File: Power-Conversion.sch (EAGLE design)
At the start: 25 parts, among them Q1 SUM90P10-19L, U7 LM2678

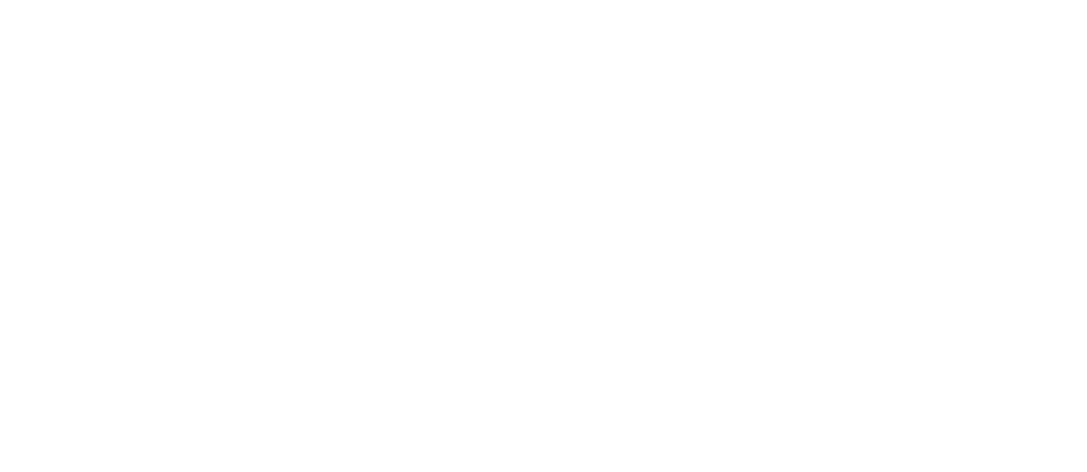
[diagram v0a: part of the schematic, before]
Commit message: added current sense
added current sense and support things
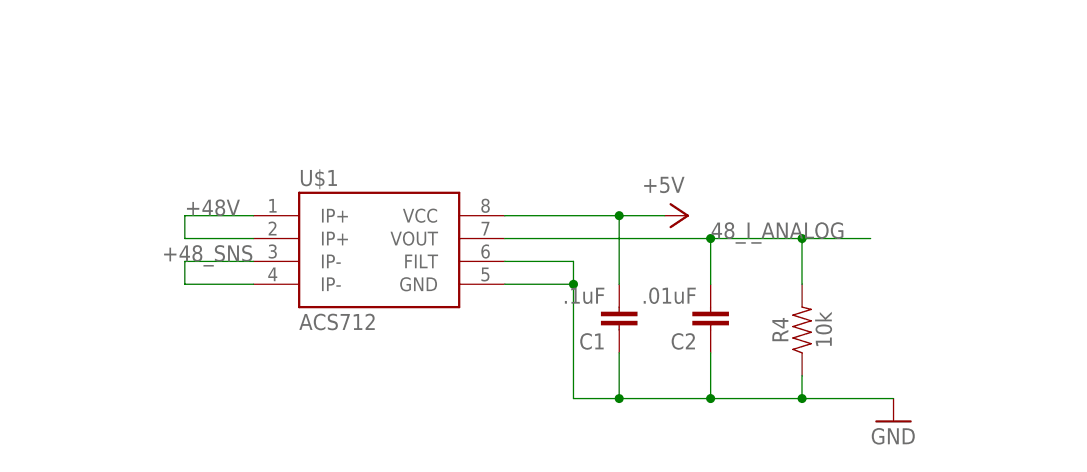
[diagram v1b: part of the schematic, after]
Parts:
- added C1: .1uF, SparkFun-Capacitors:4.7UF0603
- added C2: .01uF, SparkFun-Capacitors:4.7UF0603
- added R4: 10k, SparkFun-Resistors:10KOHM-0603-1/10W-1%
- added U$1: ACS712, SparkFun-Sensors:ACS712
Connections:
- new net +48_SNS: U$1.IP-@3, U$1.IP-@4
- new net 48_I_ANALOG: C2.2, R4.2, U$1.VOUT
- net +48V: now also U$1.IP+@1, U$1.IP+@2
- net +5V: now also C1.2, U$1.VCC
- net GND: now also C1.1, C2.1, R4.1, U$1.FILT, U$1.GND
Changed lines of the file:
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@@
 <attribute name="PARTNO" value="SUM90P10-19L-E3CT-ND"/>
 </part>
+<part name="U$1" library="SparkFun-Sensors" deviceset="ACS712" device="" value="ACS712"/>
+<part name="C1" library="SparkFun-Capacitors" deviceset="4.7UF" device="0603" value=".1uF"/>
+<part name="C2" library="SparkFun-Capacitors" deviceset="4.7UF" device="0603" value=".01uF"/>
+<part name="R4" library="SparkFun-Resistors" deviceset="10KOHM" device="-0603-1/10W-1%" value="10k"/>
+<part name="GND2" library="supply1" deviceset="GND" device=""/>
+<part name="P+5" library="supply1" deviceset="+5V" device=""/>
 </parts>
 <sheets>
@@
 <attribute name="BOM" value="INCLUDE" x="116.84" y="193.04" size="0.0254" layer="96" font="vector" rot="MR0" display="off"/>
 </instance>
+<instance part="U$1" gate="G$1" x="147.32" y="109.22"/>
+<instance part="C1" gate="G$1" x="172.72" y="104.14" rot="R180"/>
+<instance part="C2" gate="G$1" x="182.88" y="104.14" rot="R180"/>
+<instance part="R4" gate="G$1" x="193.04" y="101.6" rot="R90"/>
+<instance part="GND2" gate="1" x="203.2" y="91.44"/>
+<instance part="P+5" gate="1" x="180.34" y="114.3" rot="R270"/>
 </instances>
 <busses>
@@
 <pinref part="GND1" gate="1" pin="GND"/>
 </segment>
+<segment>
+<pinref part="U$1" gate="G$1" pin="GND"/>
+<wire x1="160.02" y1="106.68" x2="167.64" y2="106.68" width="0.1524" layer="91"/>
+<wire x1="167.64" y1="106.68" x2="167.64" y2="93.98" width="0.1524" layer="91"/>
+<pinref part="GND2" gate="1" pin="GND"/>
+<wire x1="167.64" y1="93.98" x2="172.72" y2="93.98" width="0.1524" layer="91"/>
+<wire x1="172.72" y1="93.98" x2="182.88" y2="93.98" width="0.1524" layer="91"/>
+<pinref part="U$1" gate="G$1" pin="FILT"/>
+<wire x1="182.88" y1="93.98" x2="193.04" y2="93.98" width="0.1524" layer="91"/>
+<wire x1="193.04" y1="93.98" x2="203.2" y2="93.98" width="0.1524" layer="91"/>
+<wire x1="160.02" y1="109.22" x2="167.64" y2="109.22" width="0.1524" layer="91"/>
+<wire x1="167.64" y1="109.22" x2="167.64" y2="106.68" width="0.1524" layer="91"/>
+<pinref part="C1" gate="G$1" pin="1"/>
+<wire x1="172.72" y1="93.98" x2="172.72" y2="99.06" width="0.1524" layer="91"/>
+<pinref part="C2" gate="G$1" pin="1"/>
+<wire x1="182.88" y1="99.06" x2="182.88" y2="93.98" width="0.1524" layer="91"/>
+<pinref part="R4" gate="G$1" pin="1"/>
+<wire x1="193.04" y1="96.52" x2="193.04" y2="93.98" width="0.1524" layer="91"/>
+</segment>
 </net>
 <net name="ONOFF" class="0">
@@
 <wire x1="238.76" y1="185.42" x2="238.76" y2="177.8" width="0.1524" layer="91"/>
 </segment>
+<segment>
+<pinref part="U$1" gate="G$1" pin="VCC"/>
+<pinref part="P+5" gate="1" pin="+5V"/>
+<wire x1="160.02" y1="114.3" x2="172.72" y2="114.3" width="0.1524" layer="91"/>
+<pinref part="C1" gate="G$1" pin="2"/>
+<wire x1="172.72" y1="114.3" x2="177.8" y2="114.3" width="0.1524" layer="91"/>
+<wire x1="172.72" y1="106.68" x2="172.72" y2="114.3" width="0.1524" layer="91"/>
+</segment>
 </net>
 <net name="N$25" class="0">
@@
 <wire x1="121.92" y1="195.58" x2="129.54" y2="195.58" width="0.1524" layer="91"/>
 <label x="134.62" y="195.58" size="1.778" layer="95"/>
+</segment>
+<segment>
+<pinref part="U$1" gate="G$1" pin="IP+@1"/>
+<wire x1="132.08" y1="114.3" x2="124.46" y2="114.3" width="0.1524" layer="91"/>
+<pinref part="U$1" gate="G$1" pin="IP+@2"/>
+<wire x1="132.08" y1="111.76" x2="124.46" y2="111.76" width="0.1524" layer="91"/>
+<wire x1="124.46" y1="114.3" x2="124.46" y2="111.76" width="0.1524" layer="91"/>
+<label x="124.46" y="114.3" size="1.778" layer="95"/>
 </segment>
 </net>
@@
 </segment>
 </net>
+<net name="+48_SNS" class="0">
+<segment>
+<pinref part="U$1" gate="G$1" pin="IP-@3"/>
+<wire x1="132.08" y1="109.22" x2="124.46" y2="109.22" width="0.1524" layer="91"/>
+<pinref part="U$1" gate="G$1" pin="IP-@4"/>
+<wire x1="132.08" y1="106.68" x2="124.46" y2="106.68" width="0.1524" layer="91"/>
+<wire x1="124.46" y1="109.22" x2="124.46" y2="106.68" width="0.1524" layer="91"/>
+<label x="121.92" y="109.22" size="1.778" layer="95"/>
+</segment>
+</net>
+<net name="48_I_ANALOG" class="0">
+<segment>
+<pinref part="U$1" gate="G$1" pin="VOUT"/>
+<wire x1="160.02" y1="111.76" x2="182.88" y2="111.76" width="0.1524" layer="91"/>
+<label x="182.88" y="111.76" size="1.778" layer="95"/>
+<pinref part="C2" gate="G$1" pin="2"/>
+<wire x1="182.88" y1="111.76" x2="193.04" y2="111.76" width="0.1524" layer="91"/>
+<wire x1="193.04" y1="111.76" x2="200.66" y2="111.76" width="0.1524" layer="91"/>
+<wire x1="182.88" y1="106.68" x2="182.88" y2="111.76" width="0.1524" layer="91"/>
+<pinref part="R4" gate="G$1" pin="2"/>
+<wire x1="193.04" y1="106.68" x2="193.04" y2="111.76" width="0.1524" layer="91"/>
+</segment>
+</net>
+<net name="GND1" class="0">
+<segment>
+<junction x="172.72" y="114.3"/>
+</segment>
+</net>
+<net name="GND2" class="0">
+<segment>
+<junction x="172.72" y="93.98"/>
+</segment>
+</net>
+<net name="GND3" class="0">
+<segment>
+<junction x="182.88" y="93.98"/>
+</segment>
+</net>
+<net name="GND4" class="0">
+<segment>
+<junction x="182.88" y="111.76"/>
+</segment>
+</net>
+<net name="GND5" class="0">
+<segment>
+<junction x="193.04" y="111.76"/>
+</segment>
+</net>
+<net name="GND6" class="0">
+<segment>
+<junction x="193.04" y="93.98"/>
+</segment>
+</net>
+<net name="GND7" class="0">
+<segment>
+<junction x="167.64" y="106.68"/>
+</segment>
+</net>

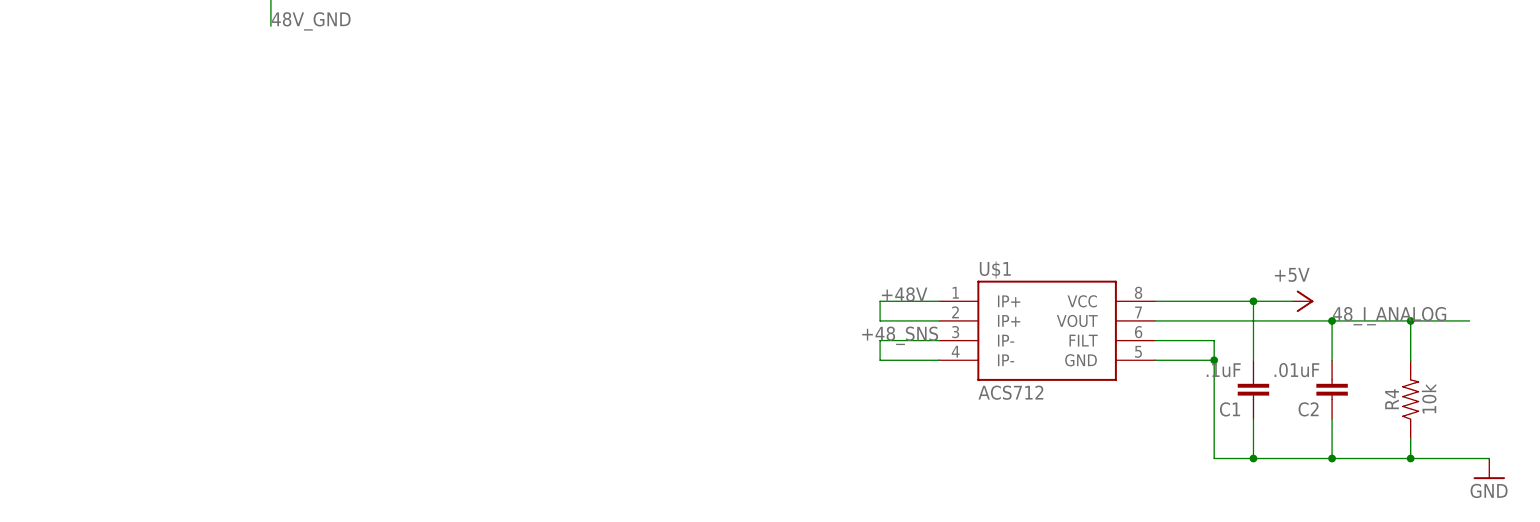
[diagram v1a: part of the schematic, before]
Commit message: Added voltage connectors
added the voltage connectors
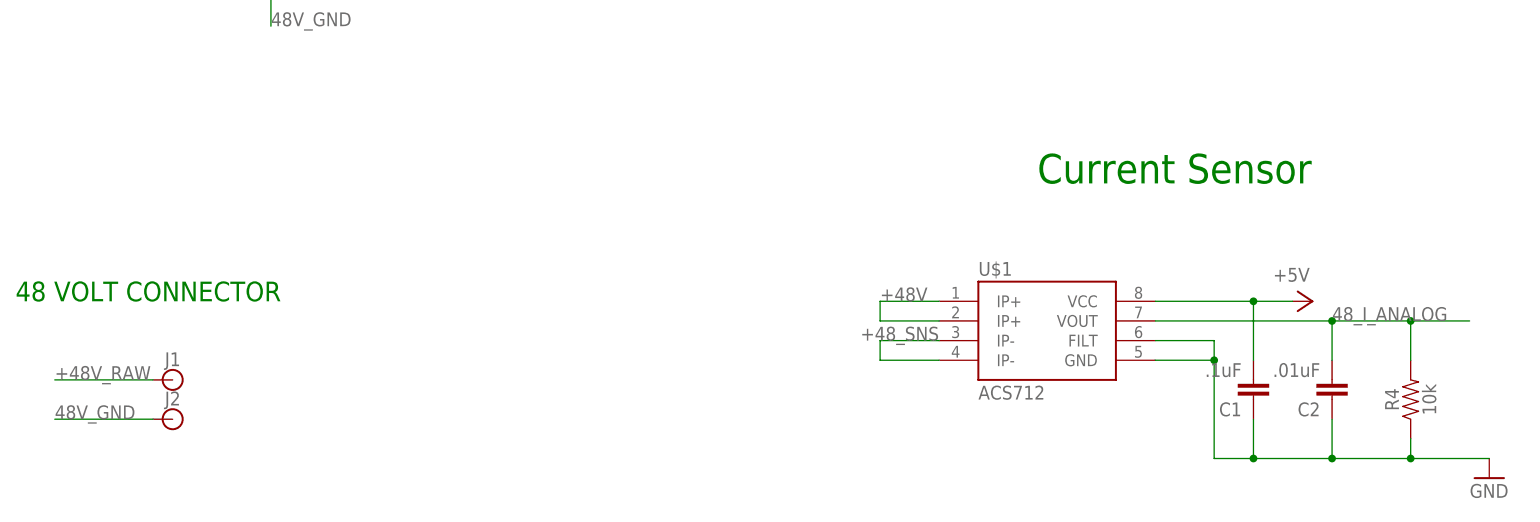
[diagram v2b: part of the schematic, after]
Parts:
- added J1, J2: (no value), SparkFun-Connectors:BANANA_CONN
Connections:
- net +48V_RAW: now also J1.1
- net 48V_GND: now also J2.1
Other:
- note added: "48 VOLT CONNECTOR"
- note added: "Current Sensor"
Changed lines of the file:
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@@
 <part name="GND2" library="supply1" deviceset="GND" device=""/>
 <part name="P+5" library="supply1" deviceset="+5V" device=""/>
+<part name="J1" library="SparkFun-Connectors" deviceset="BANANA_CONN" device=""/>
+<part name="J2" library="SparkFun-Connectors" deviceset="BANANA_CONN" device=""/>
 </parts>
 <sheets>
@@
 <text x="20.32" y="205.74" size="3.81" layer="91">Turn on switch</text>
 <text x="96.52" y="210.82" size="3.81" layer="91">reverse voltage protection</text>
+<text x="12.7" y="114.3" size="2.54" layer="91">48 VOLT CONNECTOR</text>
+<text x="144.78" y="129.54" size="3.81" layer="91">Current Sensor</text>
 </plain>
 <instances>
@@
 <instance part="GND2" gate="1" x="203.2" y="91.44"/>
 <instance part="P+5" gate="1" x="180.34" y="114.3" rot="R270"/>
+<instance part="J1" gate="G$1" x="33.02" y="104.14"/>
+<instance part="J2" gate="G$1" x="33.02" y="99.06"/>
 </instances>
 <busses>
@@
 <label x="119.38" y="157.48" size="1.778" layer="95"/>
 </segment>
+<segment>
+<pinref part="J2" gate="G$1" pin="1"/>
+<wire x1="30.48" y1="99.06" x2="17.78" y2="99.06" width="0.1524" layer="91"/>
+<label x="17.78" y="99.06" size="1.778" layer="95"/>
+</segment>
 </net>
 <net name="+12V" class="0">
@@
 <label x="99.06" y="203.2" size="1.778" layer="95"/>
 </segment>
-</net>
+<segment>
+<pinref part="J1" gate="G$1" pin="1"/>
+<wire x1="30.48" y1="104.14" x2="17.78" y2="104.14" width="0.1524" layer="91"/>
+<label x="17.78" y="104.14" size="1.778" layer="95"/>
+</segment>
+</net>

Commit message: added Connectors
added connectors to schematic
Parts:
- added U$2: SAMTEC-10, SAMTEC-10:SAMTEC-10
- added U$3, U$8: POWER-BRICK-CONNECTOR, MotherboardParts:POWER-BRICK-CONNECTOR
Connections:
- new net 12V: U$3.P$2, U$8.P$1
- net GND: now also U$3.P$1, U$8.P$2
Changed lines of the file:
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@@
 <part name="J1" library="SparkFun-Connectors" deviceset="BANANA_CONN" device=""/>
 <part name="J2" library="SparkFun-Connectors" deviceset="BANANA_CONN" device=""/>
+<part name="U$3" library="MotherboardParts" deviceset="POWER-BRICK-CONNECTOR" device=""/>
+<part name="U$8" library="MotherboardParts" deviceset="POWER-BRICK-CONNECTOR" device=""/>
+<part name="GND3" library="supply1" deviceset="GND" device=""/>
+<part name="GND4" library="supply1" deviceset="GND" device=""/>
+<part name="SUPPLY1" library="SparkFun-PowerSymbols" deviceset="12V" device=""/>
+<part name="SUPPLY2" library="SparkFun-PowerSymbols" deviceset="12V" device=""/>
+<part name="U$2" library="SAMTEC-10" deviceset="SAMTEC-10" device=""/>
 </parts>
 <sheets>
@@
 <instance part="R4" gate="G$1" x="193.04" y="101.6" rot="R90"/>
 <instance part="GND2" gate="1" x="203.2" y="91.44"/>
-<instance part="P+5" gate="1" x="180.34" y="114.3" rot="R270"/>
+<instance part="P+5" gate="1" x="172.72" y="124.46"/>
 <instance part="J1" gate="G$1" x="33.02" y="104.14"/>
 <instance part="J2" gate="G$1" x="33.02" y="99.06"/>
+<instance part="U$3" gate="G$1" x="83.82" y="421.64"/>
+<instance part="U$8" gate="G$1" x="83.82" y="452.12"/>
+<instance part="GND3" gate="1" x="101.6" y="421.64"/>
+<instance part="GND4" gate="1" x="101.6" y="436.88"/>
+<instance part="SUPPLY1" gate="G$1" x="109.22" y="421.64"/>
+<instance part="SUPPLY2" gate="G$1" x="109.22" y="464.82"/>
+<instance part="U$2" gate="G$1" x="81.28" y="492.76"/>
 </instances>
 <busses>
@@
 <wire x1="193.04" y1="96.52" x2="193.04" y2="93.98" width="0.1524" layer="91"/>
 </segment>
+<segment>
+<pinref part="U$8" gate="G$1" pin="P$2"/>
+<wire x1="96.52" y1="444.5" x2="101.6" y2="444.5" width="0.1524" layer="91"/>
+<pinref part="GND4" gate="1" pin="GND"/>
+<wire x1="101.6" y1="444.5" x2="101.6" y2="439.42" width="0.1524" layer="91"/>
+</segment>
+<segment>
+<pinref part="U$3" gate="G$1" pin="P$1"/>
+<wire x1="96.52" y1="429.26" x2="101.6" y2="429.26" width="0.1524" layer="91"/>
+<pinref part="GND3" gate="1" pin="GND"/>
+<wire x1="101.6" y1="429.26" x2="101.6" y2="424.18" width="0.1524" layer="91"/>
+</segment>
 </net>
 <net name="ONOFF" class="0">
@@
 <wire x1="160.02" y1="114.3" x2="172.72" y2="114.3" width="0.1524" layer="91"/>
 <pinref part="C1" gate="G$1" pin="2"/>
-<wire x1="172.72" y1="114.3" x2="177.8" y2="114.3" width="0.1524" layer="91"/>
+<wire x1="172.72" y1="114.3" x2="172.72" y2="121.92" width="0.1524" layer="91"/>
 <wire x1="172.72" y1="106.68" x2="172.72" y2="114.3" width="0.1524" layer="91"/>
 </segment>
@@
 </segment>
 </net>
+<net name="12V" class="0">
+<segment>
+<pinref part="U$3" gate="G$1" pin="P$2"/>
+<wire x1="96.52" y1="414.02" x2="109.22" y2="414.02" width="0.1524" layer="91"/>
+<pinref part="SUPPLY1" gate="G$1" pin="12V"/>
+<wire x1="109.22" y1="414.02" x2="109.22" y2="421.64" width="0.1524" layer="91"/>
+</segment>
+<segment>
+<pinref part="U$8" gate="G$1" pin="P$1"/>
+<wire x1="96.52" y1="459.74" x2="109.22" y2="459.74" width="0.1524" layer="91"/>
+<pinref part="SUPPLY2" gate="G$1" pin="12V"/>
+<wire x1="109.22" y1="459.74" x2="109.22" y2="464.82" width="0.1524" layer="91"/>
+</segment>
+</net>

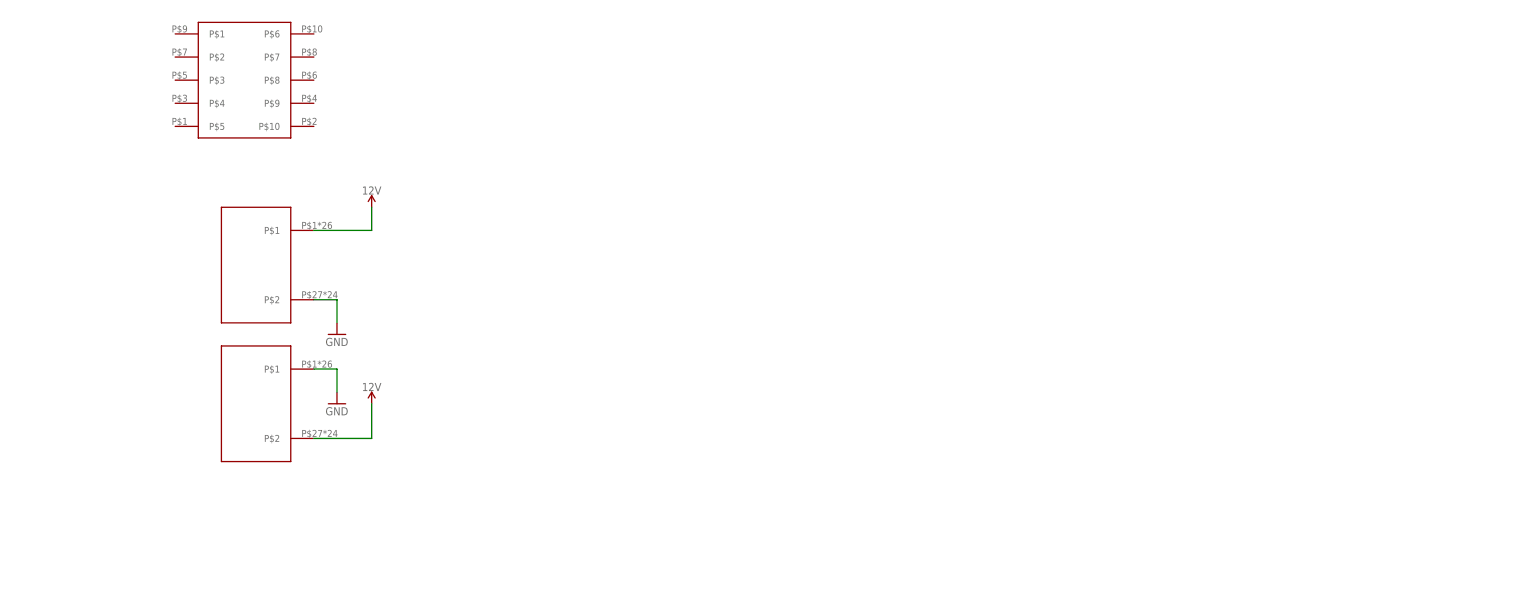
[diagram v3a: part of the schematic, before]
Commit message: Added micro
added the microcontroller.
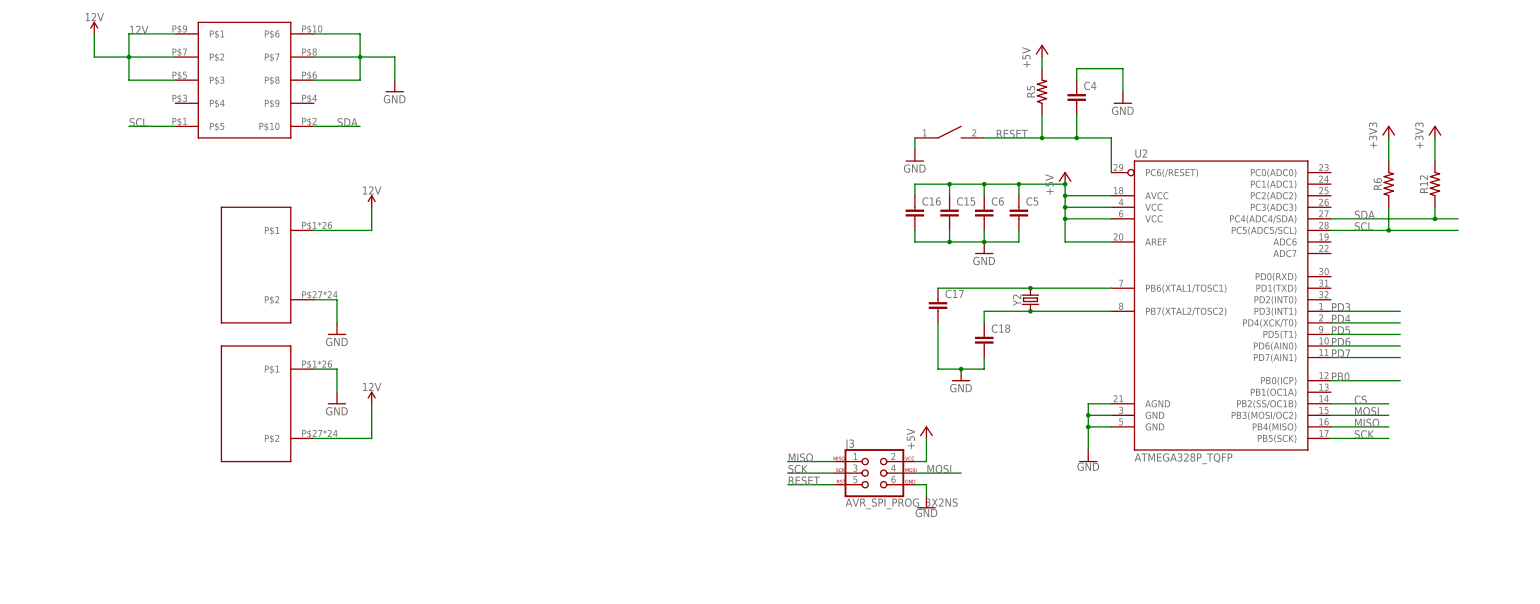
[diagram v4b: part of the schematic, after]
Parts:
- added C15, C16, C17, C18, C4, C5, C6: (no value), rcl:C-EUC0603
- added J3: AVR_SPI_PROG_3X2NS, SparkFun-Connectors:AVR_SPI_PROG_3X2NS
- added R12, R5, R6: (no value), SparkFun-Resistors:RESISTOR0603
- added RESET: SWITCH, DiscreteComponents:SWITCH
- added U2: ATMEGA328P_TQFP, SparkFun-IC-Microcontroller:ATMEGA328P_TQFP
- added Y2: (no value), SparkFun-Clocks:CRYSTALPTH-HC49US
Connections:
- new net +3V3: R12.2, R6.2
- new net CS: U2.PB2(SS/OC1B)
- new net MISO: J3.1, U2.PB4(MISO)
- new net MOSI: J3.4, U2.PB3(MOSI/OC2)
- new net N$14: C17.1, U2.PB6(XTAL1/TOSC1), Y2.2
- new net N$15: C18.1, U2.PB7(XTAL2/TOSC2), Y2.1
- new net PB0: U2.PB0(ICP)
- new net PD3: U2.PD3(INT1)
- new net PD4: U2.PD4(XCK/T0)
- new net PD5: U2.PD5(T1)
- new net PD6: U2.PD6(AIN0)
- new net PD7: U2.PD7(AIN1)
- new net RESET: C4.2, J3.5, R5.1, RESET.P$2, U2.PC6(/RESET)
- new net SCK: J3.3, U2.PB5(SCK)
- new net SCL: R6.1, U$2.P$5, U2.PC5(ADC5/SCL)
- new net SDA: R12.1, U$2.P$10, U2.PC4(ADC4/SDA)
- net +5V: now also C15.1, C16.1, C5.1, C6.1, J3.2, R5.2, U2.AREF, U2.AVCC, U2.VCC@4, U2.VCC@6
- net 12V: now also U$2.P$1, U$2.P$2, U$2.P$3
- net GND: now also C15.2, C16.2, C17.2, C18.2, C4.1, C5.2, C6.2, J3.6, RESET.P$1, U$2.P$6, U$2.P$7, U$2.P$8, U2.AGND, U2.GND@3, U2.GND@5

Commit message: Added Connectors
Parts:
- added U$11, U$12, U$13: POWER_BRICK_CONNECTORS(2X15), MotherBoardParts2:POWER_BRICK_CONNECTORS(2X15)
- added U$14, U$15, U$16: POWER_BRICK_CONNECTORS(2X6), MotherBoardParts2:POWER_BRICK_CONNECTORS(2X6)
- added U1: LM1085IS-3.3, PowerComponents:LM1085IS-3.3
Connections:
- new net +48_RAW: J1.1
- new net 48_GND: J2.1
- net +48V_RAW: no longer J1.1
- net 48V_GND: no longer J2.1
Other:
- moved on the sheet: C15, C16, C17, C18, C4, C5, C6, J3, R12, R5, R6, U2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
